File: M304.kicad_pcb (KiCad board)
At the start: 2 copper layers, 170.7 x 170 mm, 121 parts, among them J1 LCD 2004, J2 Relay OUT, J3 iM920, J4 GPS, J5 POWER IN, P1 Digital, P10 CONN_01X01, P11 CONN_01X01, P12 CONN_01X01, P13 CONN_01X01, P2 Power, P3 Analog, P4 Analog, P5 PWM, P6 PWM, P7 Communication, P8 CONN_01X01, P9 CONN_01X01, SW1 RESET, SW2 SW_A, SW2-1 SW_SPDT, SW2-2 SW_SPDT, SW2-3 SW_SPDT, SW2-4 SW_SPDT, SW2-5 SW_SPDT, SW2-6 SW_SPDT, SW2-7 SW_SPDT, SW2-8 SW_SPDT, SW2-9 MS611F, SW3 SW_B, SW4 SW_C, SW5 SW_D, SW6 SW_ENTER, SW7 SAFEMODE, U1 DS1307+, U2 24LC256, U2-1 TLP222G-2, U2-2 TLP222G-2, U2-3 TLP222G-2, U2-4 TLP222G-2, U2-5 TLP222G-2, U2-6 TLP222G-2, U2-7 TLP222G-2, U2-8 TLP222G-2, U3 W5500, Y1 32.768kHz

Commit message: PCB設計中
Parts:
- SW2: value SW_A -> UP
- SW3: value SW_B -> DOWN
- SW4: value SW_C -> LEFT
- SW5: value SW_D -> RIGHT
- SW6: value SW_ENTER -> ENTER
- moved SW1 156.8 mm to (95.0, 117.3), turned to -90 degrees
- moved JD30 134.9 mm to (255.9, 76.2)
- moved JD49 118.2 mm to (255.9, 91.4)
- moved JD48 117.9 mm to (255.9, 86.4)
- moved SW2-5 115.0 mm to (182.9, 134.4), turned to 90 degrees
- moved SW2-8 109.5 mm to (182.9, 141.1), turned to 90 degrees
- moved SW2-1 104.6 mm to (182.9, 147.8), turned to 90 degrees
- moved JD31 102.3 mm to (255.9, 81.3)
- moved SW2-2 100.3 mm to (182.9, 154.5), turned to 90 degrees
- moved SW2-6 96.8 mm to (182.9, 161.2), turned to 90 degrees
- moved SW2-4 93.4 mm to (192.2, 147.8), turned to 90 degrees
- moved SW2-3 88.6 mm to (192.2, 154.5), turned to 90 degrees
- moved D3 87.7 mm to (171.2, 86.5)
- moved SW7 87.2 mm to (181.9, 184.4)
- moved SW2-7 84.6 mm to (192.2, 161.2), turned to 90 degrees
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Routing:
- net /4(**): track 0.00 -> 173.5 mm
- net /17(Rx2): track 0.00 -> 172.5 mm, vias 0 -> 2
- net /15(Rx3): track 0.00 -> 168.9 mm, vias 0 -> 2
- net /16(Tx2): track 0.00 -> 158.0 mm, vias 0 -> 2
- net /51(MOSI): track 0.00 -> 139.5 mm, vias 0 -> 2
- net /52(SCK): track 0.00 -> 124.3 mm, vias 0 -> 2
- net /53(SS): track 0.00 -> 124.0 mm, vias 0 -> 2
- net Net-(D2-Pad2): track 15.2 -> 98.2 mm
- net /35: track 0.00 -> 82.6 mm
- net +3V3: track 179.9 -> 261.7 mm, vias 0 -> 2
- net /48: track 0.00 -> 72.6 mm
- net /36: track 0.00 -> 68.7 mm
- net /49: track 0.00 -> 65.3 mm
- net /30: track 0.00 -> 64.9 mm, vias 0 -> 1
- net /31: track 0.00 -> 59.2 mm, vias 0 -> 1
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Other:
- board text added: "+"
- board text added: "GND"
- board text added: "SELECTOR"

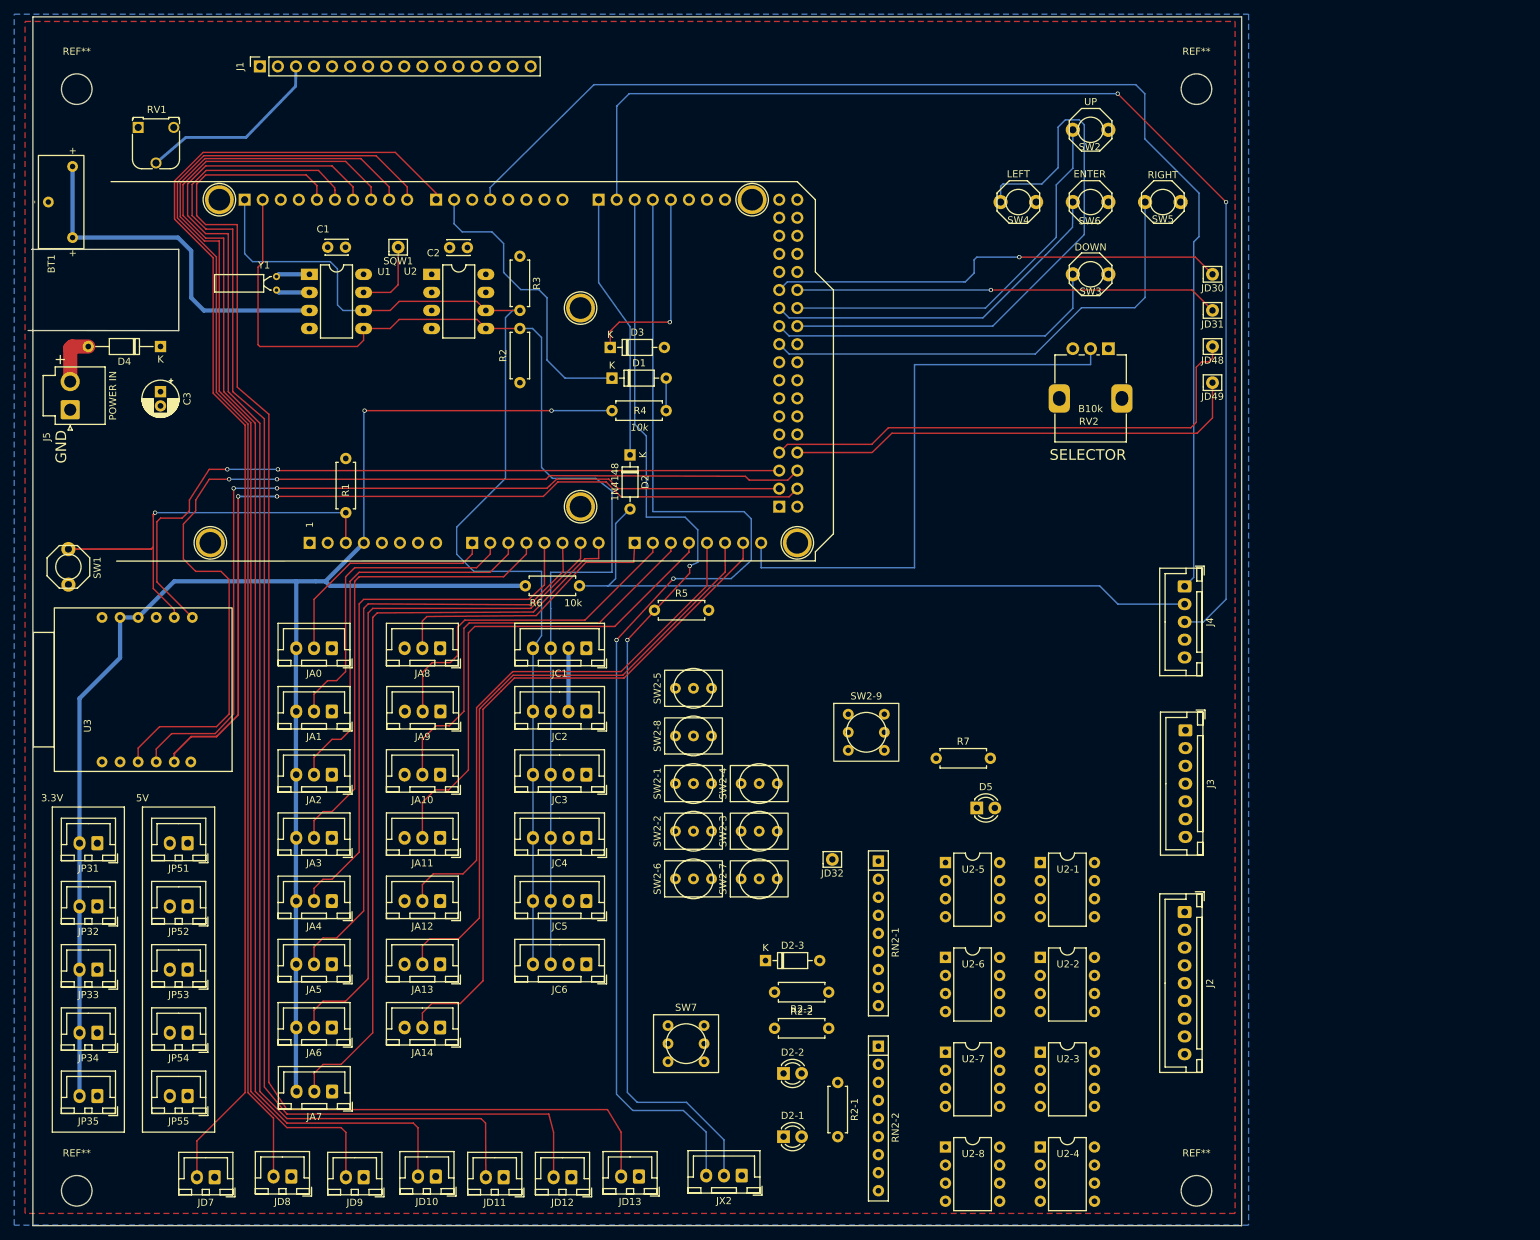
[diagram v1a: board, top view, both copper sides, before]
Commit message: W5500周囲の変更
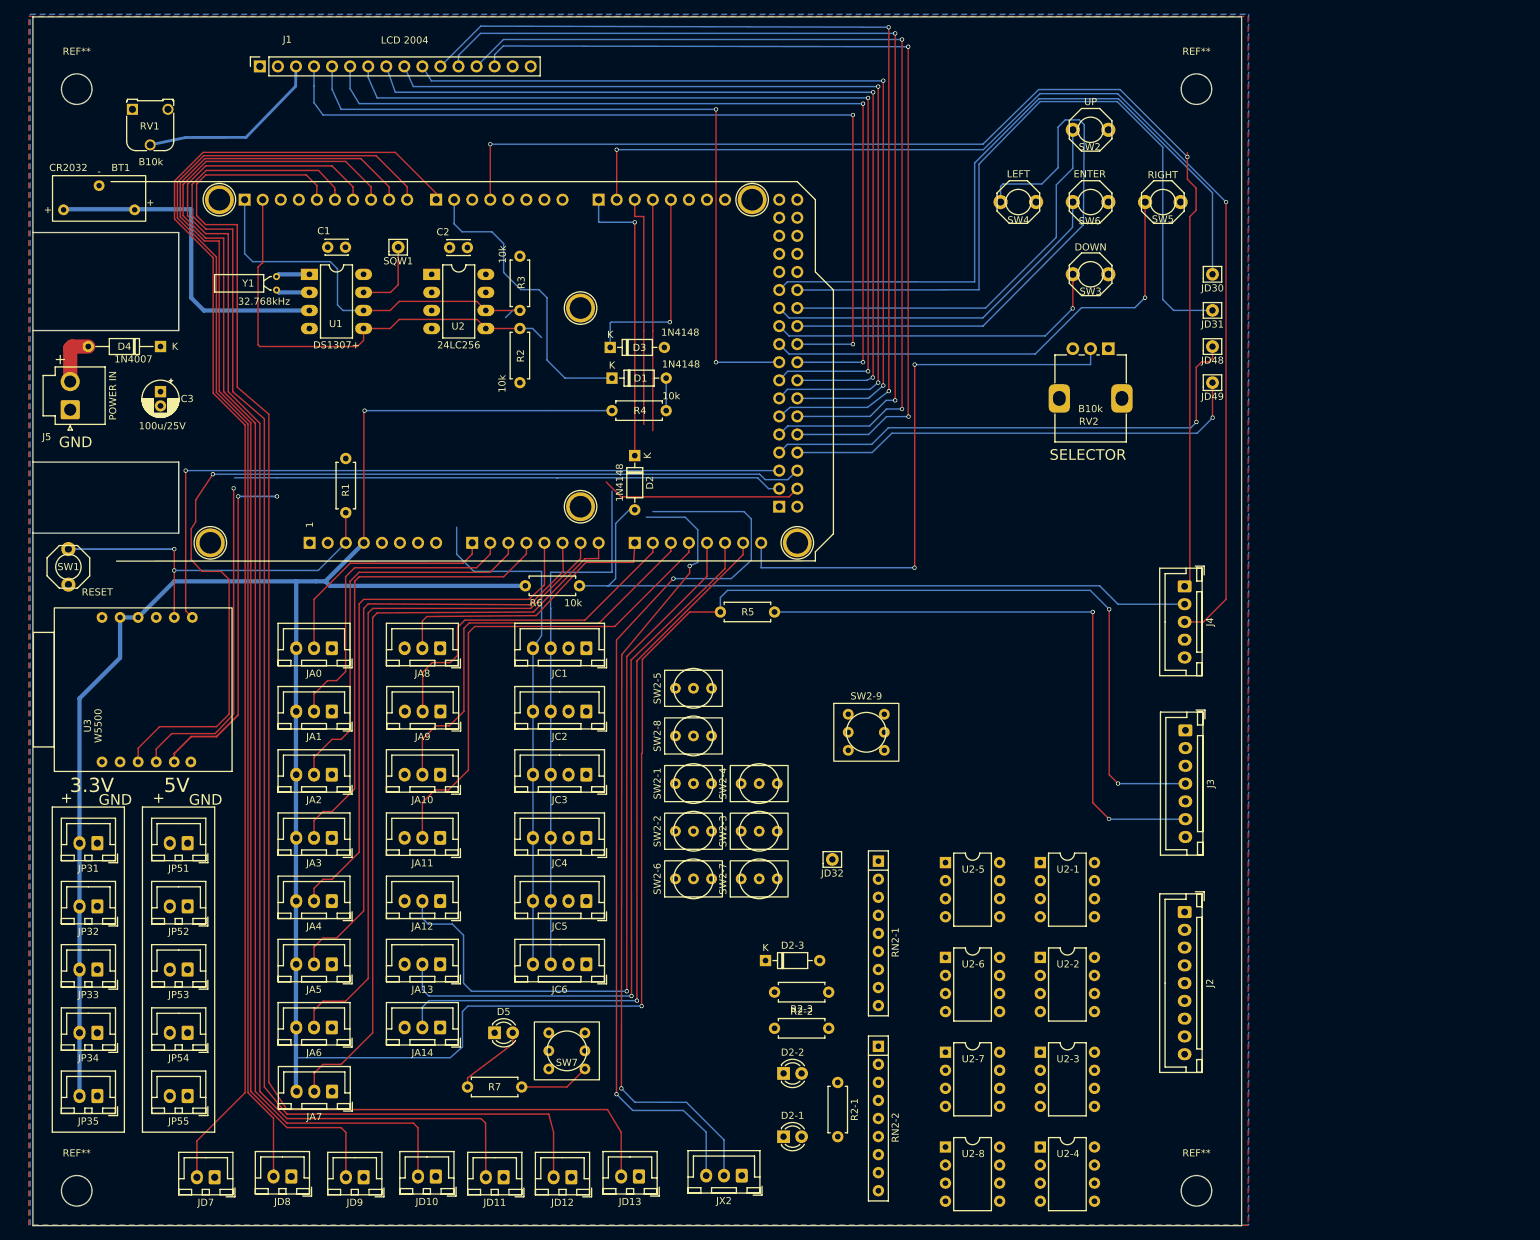
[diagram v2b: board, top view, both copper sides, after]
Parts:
- D4: value D -> 1N4007
- moved D5 74.8 mm to (154.9, 182.9)
- moved R7 74.4 mm to (158.8, 190.5), turned to 180 degrees
- moved SW7 16.8 mm to (165.1, 185.4), turned to 180 degrees
- moved R5 9.27 mm to (186.7, 123.7)
- moved BT1 5.36 mm to (99.3, 65.5), turned to 0 degrees
- moved RV1 2.67 mm to (104.0, 53.0)
- moved D2 0.67 mm to (174.7, 101.7)
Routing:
- net +3V3: track 261.7 -> 471.6 mm, vias 2 -> 4
- net /44: track 0.00 -> 133.3 mm, vias 0 -> 2
- net /46: track 0.00 -> 132.1 mm, vias 0 -> 2
- net /45: track 0.00 -> 130.6 mm, vias 0 -> 2
- net /47: track 0.00 -> 129.1 mm, vias 0 -> 2
- net /40: track 0.00 -> 125.2 mm, vias 0 -> 2
- net /42: track 0.00 -> 124.9 mm, vias 0 -> 2
- net /39: track 0.00 -> 122.1 mm, vias 0 -> 2
- net /41: track 0.00 -> 121.9 mm, vias 0 -> 2
- net /37: track 0.00 -> 121.8 mm, vias 0 -> 2
- net /43: track 0.00 -> 121.6 mm, vias 0 -> 2
- net /38: track 0.00 -> 103.5 mm, vias 0 -> 2
- net Net-(D3-Pad2): track 0.00 -> 85.8 mm, vias 0 -> 2
- net /53(SS): track 124.0 -> 76.8 mm
- net /31: track 59.2 -> 104.5 mm, vias 1 -> 0
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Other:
- board size 170.7 x 170 mm -> 170 x 170 mm
